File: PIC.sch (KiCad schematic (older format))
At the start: 0 parts

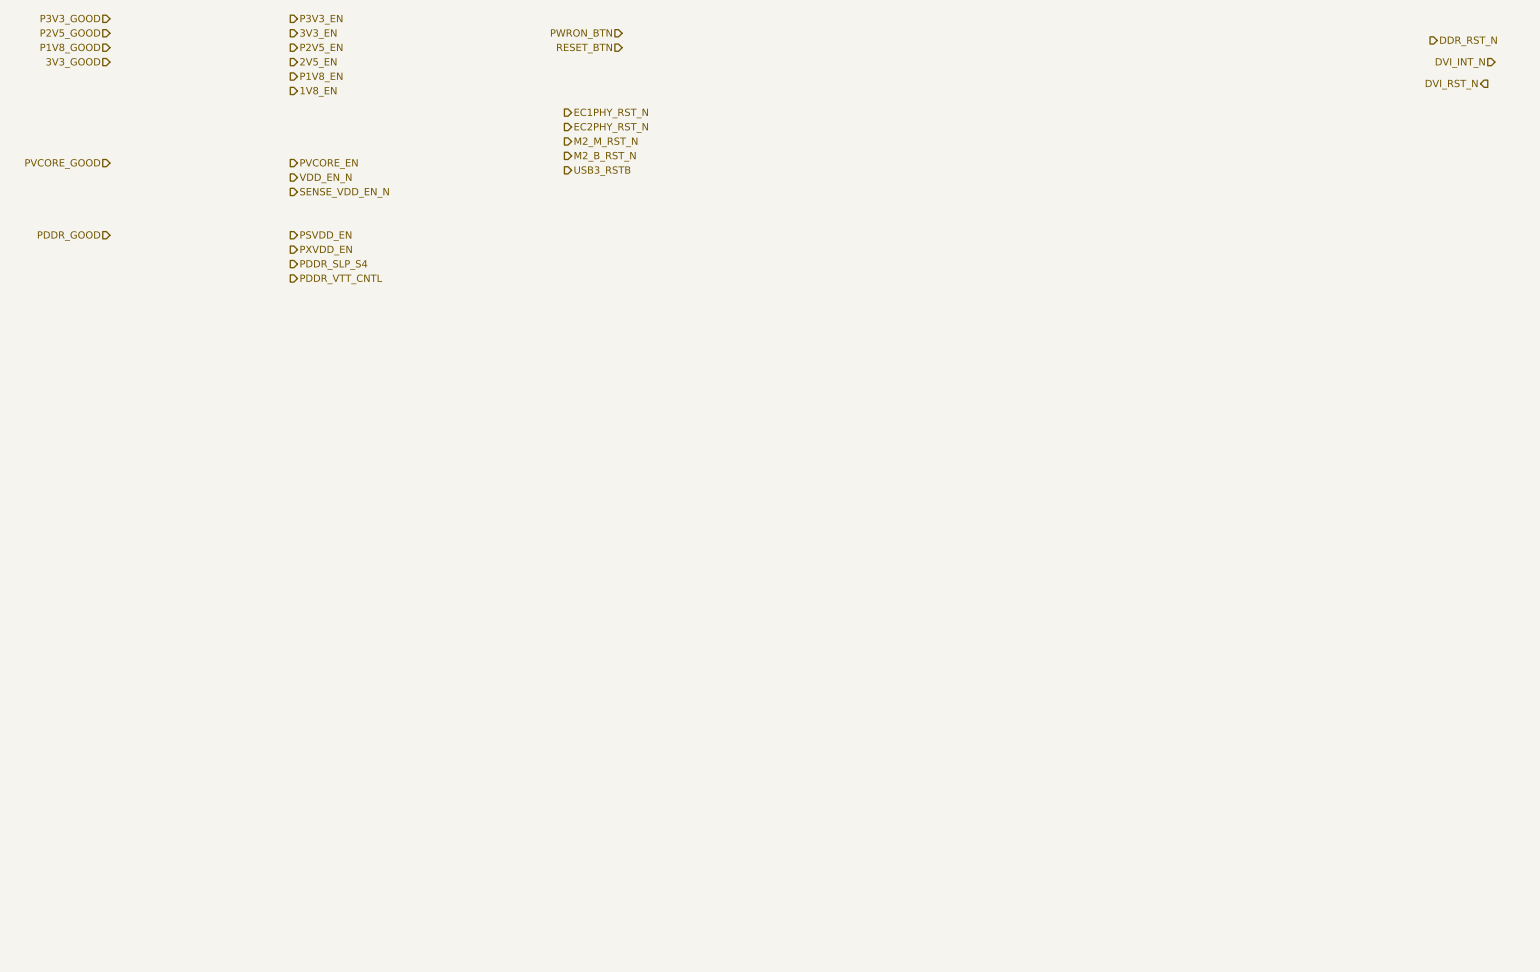
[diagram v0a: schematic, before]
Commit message: work in progress on PIC and power enable net
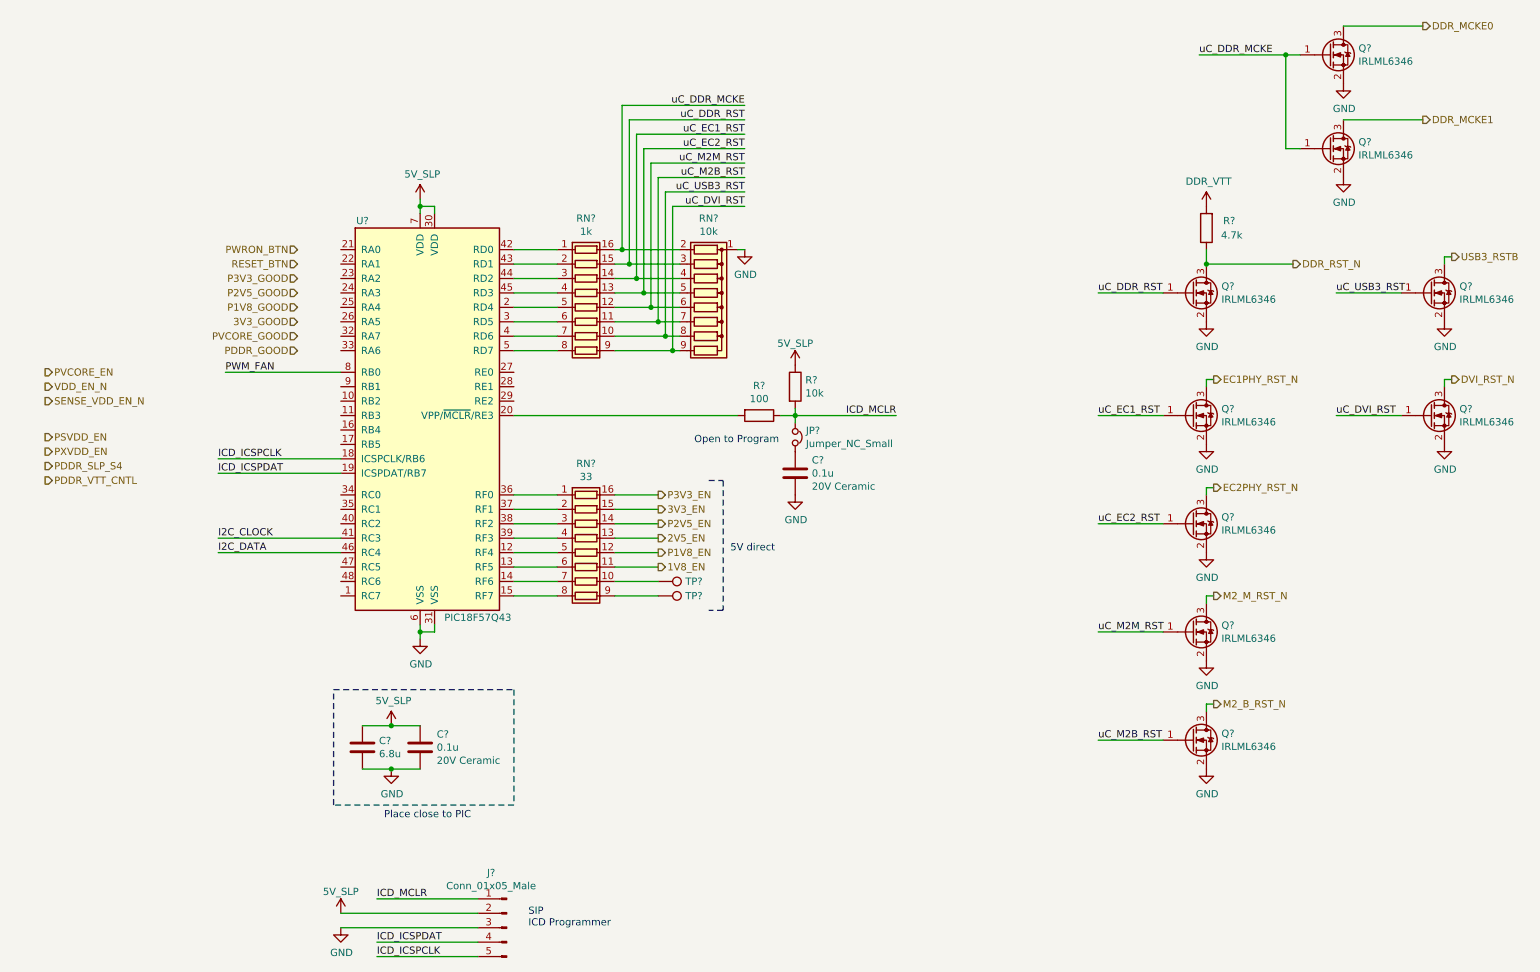
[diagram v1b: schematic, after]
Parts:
- added C? (x2): 0.1u, symbol Device:C
- added C?: 6.8u, symbol Device:C
- added J?: Conn_01x05_Male, symbol Connector:Conn_01x05_Male
- added JP?: Jumper_NC_Small, symbol Device:Jumper_NC_Small
- added Q? (x9): IRLML6346, Package_TO_SOT_SMD:SOT-23, symbol Device:Q_NMOS_GSD
- added R?: 4.7k, symbol Device:R
- added R?: 100, symbol Device:R
- added R?: 10k, symbol Device:R
- added RN?: 10k, Resistor_THT:R_Array_SIP9, symbol Device:R_Network08
- added RN?: 1k, symbol Device:R_Pack08
- added RN?: 33, symbol Device:R_Pack08
- added TP? (x2): TestPoint, symbol Connector:TestPoint
- added U?: PIC18F57Q43, Package_QFP:TQFP-48_7x7mm_P0.5mm, symbol ppc_scm:PIC18F57Q43
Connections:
- net 1V8_EN: now also RN?.11 (R6.2)
- net 2V5_EN: now also RN?.13 (R4.2)
- net 3V3_EN: now also RN?.15 (R2.2)
- net DDR_RST_N: now also Q?.3 (D), R?.1
- net DVI_RST_N: now also Q?.3 (D)
- net EC1PHY_RST_N: now also Q?.3 (D)
- net EC2PHY_RST_N: now also Q?.3 (D)
- net M2_B_RST_N: now also Q?.3 (D)
- net M2_M_RST_N: now also Q?.3 (D)
- net P1V8_EN: now also RN?.12 (R5.2)
- net P2V5_EN: now also RN?.14 (R3.2)
- net P3V3_EN: now also RN?.16 (R1.2)
- net USB3_RSTB: now also Q?.3 (D)
- new net: R?.2, U?.20 (VPP/~MCLR~/RE3)
- new net: C?.1, JP?.2
- new net: RN?.1 (R1.1), U?.42 (RD0)
- new net: RN?.2 (R2.1), U?.43 (RD1)
- new net: RN?.3 (R3.1), U?.44 (RD2)
- new net: RN?.4 (R4.1), U?.45 (RD3)
- new net: RN?.5 (R5.1), U?.2 (RD4)
- new net: RN?.6 (R6.1), U?.3 (RD5)
- new net: RN?.7 (R7.1), U?.4 (RD6)
- new net: RN?.8 (R8.1), U?.5 (RD7)
- new net: RN?.1 (R1.1), U?.36 (RF0)
- new net: RN?.10 (R7.2), TP?.1
- new net: RN?.2 (R2.1), U?.37 (RF1)
- new net: RN?.3 (R3.1), U?.38 (RF2)
- new net: RN?.4 (R4.1), U?.39 (RF3)
- new net: RN?.5 (R5.1), U?.12 (RF4)
- new net: RN?.6 (R6.1), U?.13 (RF5)
- new net: RN?.7 (R7.1), U?.14 (RF6)
- new net: RN?.8 (R8.1), U?.15 (RF7)
- new net: RN?.9 (R8.2), TP?.1
- new net 5V_SLP: C?.1, C?.1, J?.2 (Pin_2), R?.1, U?.30 (VDD), U?.7 (VDD)
- new net DDR_MCKE0: Q?.3 (D)
- new net DDR_MCKE1: Q?.3 (D)
- new net DDR_VTT: R?.2
- new net GND: C?.2, C?.2, C?.2, J?.3 (Pin_3), Q?.2 (S), Q?.2 (S), Q?.2 (S), Q?.2 (S), Q?.2 (S), Q?.2 (S), Q?.2 (S), Q?.2 (S), Q?.2 (S), RN?.1 (common), U?.31 (VSS), U?.6 (VSS)
- new net I2C_CLOCK: U?.41 (RC3)
- new net I2C_DATA: U?.46 (RC4)
- new net ICD_ICSPCLK: J?.5 (Pin_5), U?.18 (ICSPCLK/RB6)
- new net ICD_ICSPDAT: J?.4 (Pin_4), U?.19 (ICSPDAT/RB7)
- new net ICD_MCLR: J?.1 (Pin_1), JP?.1, R?.1, R?.2
- new net PWM_FAN: U?.8 (RB0)
- new net uC_DDR_MCKE: Q?.1 (G), Q?.1 (G), RN?.16 (R1.2), RN?.2 (R1)
- new net uC_DDR_RST: Q?.1 (G), RN?.15 (R2.2), RN?.3 (R2)
- new net uC_DVI_RST: Q?.1 (G), RN?.9 (R8), RN?.9 (R8.2)
- new net uC_EC1_RST: Q?.1 (G), RN?.14 (R3.2), RN?.4 (R3)
- new net uC_EC2_RST: Q?.1 (G), RN?.13 (R4.2), RN?.5 (R4)
- new net uC_M2B_RST: Q?.1 (G), RN?.11 (R6.2), RN?.7 (R6)
- new net uC_M2M_RST: Q?.1 (G), RN?.12 (R5.2), RN?.6 (R5)
- new net uC_USB3_RST: Q?.1 (G), RN?.10 (R7.2), RN?.8 (R7)
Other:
- note added: "5V direct"
- note added: "Open to Program"
- note added: "Place close to PIC"
- note added: "SIP\nICD Programmer"
